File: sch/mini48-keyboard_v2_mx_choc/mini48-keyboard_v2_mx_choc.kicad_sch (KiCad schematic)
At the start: 1 part, among them U1 Pico

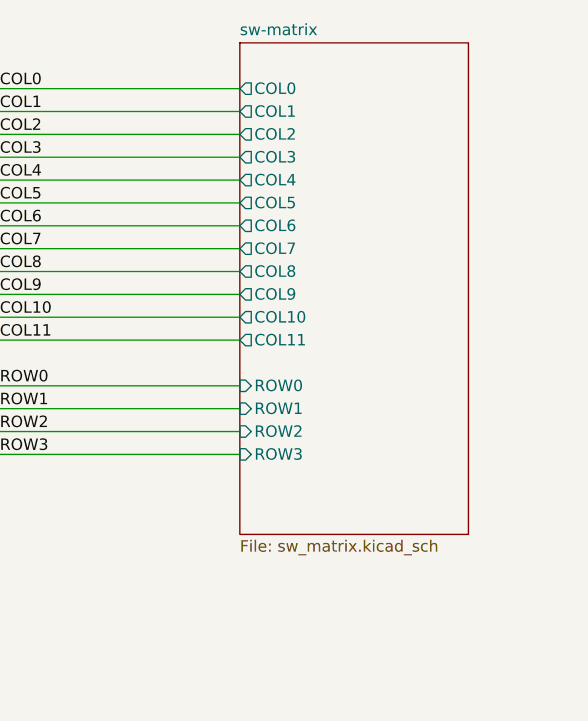
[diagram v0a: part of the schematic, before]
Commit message: スイッチのシート名を変更しました。
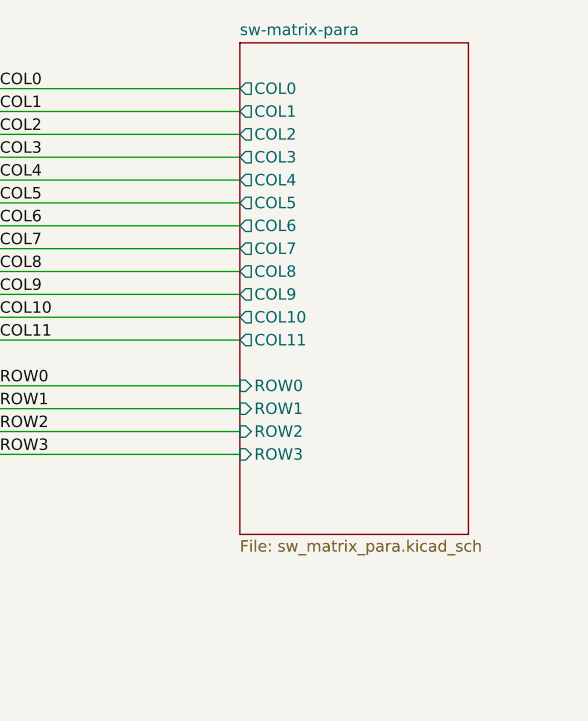
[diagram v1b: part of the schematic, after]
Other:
- sheet sw-matrix renamed sw-matrix-para
- sheet sw-matrix-para: file sw_matrix.kicad_sch -> sw_matrix_para.kicad_sch
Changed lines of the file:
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@@
 			(color 0 0 0 0.0000)
 		)
-		(property "Sheetname" "sw-matrix"
+		(property "Sheetname" "sw-matrix-para"
 			(at 204.47 36.1184 0)
 			(effects
@@
 			)
 		)
-		(property "Sheetfile" "sw_matrix.kicad_sch"
+		(property "Sheetfile" "sw_matrix_para.kicad_sch"
 			(at 204.47 92.0246 0)
 			(effects

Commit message: 基板上にUSB type-cのコネクタを実装しました。 picoのTPとジャンパ配線します。
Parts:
- added H1, H10, H11, H12, H2, H3, H4, H5, H6, H7, H8, H9: MountingHole, my_keyswitch:my_MountingHole_3.2mm_M3, symbol Mechanical:MountingHole
- U1: footprint my_pico:pico_no_dbg_th_p0.85 -> my_pico:pico_no_dbg_smd_th_p0.85
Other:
- added sheet usb type-c (usb_type_c.kicad_sch)

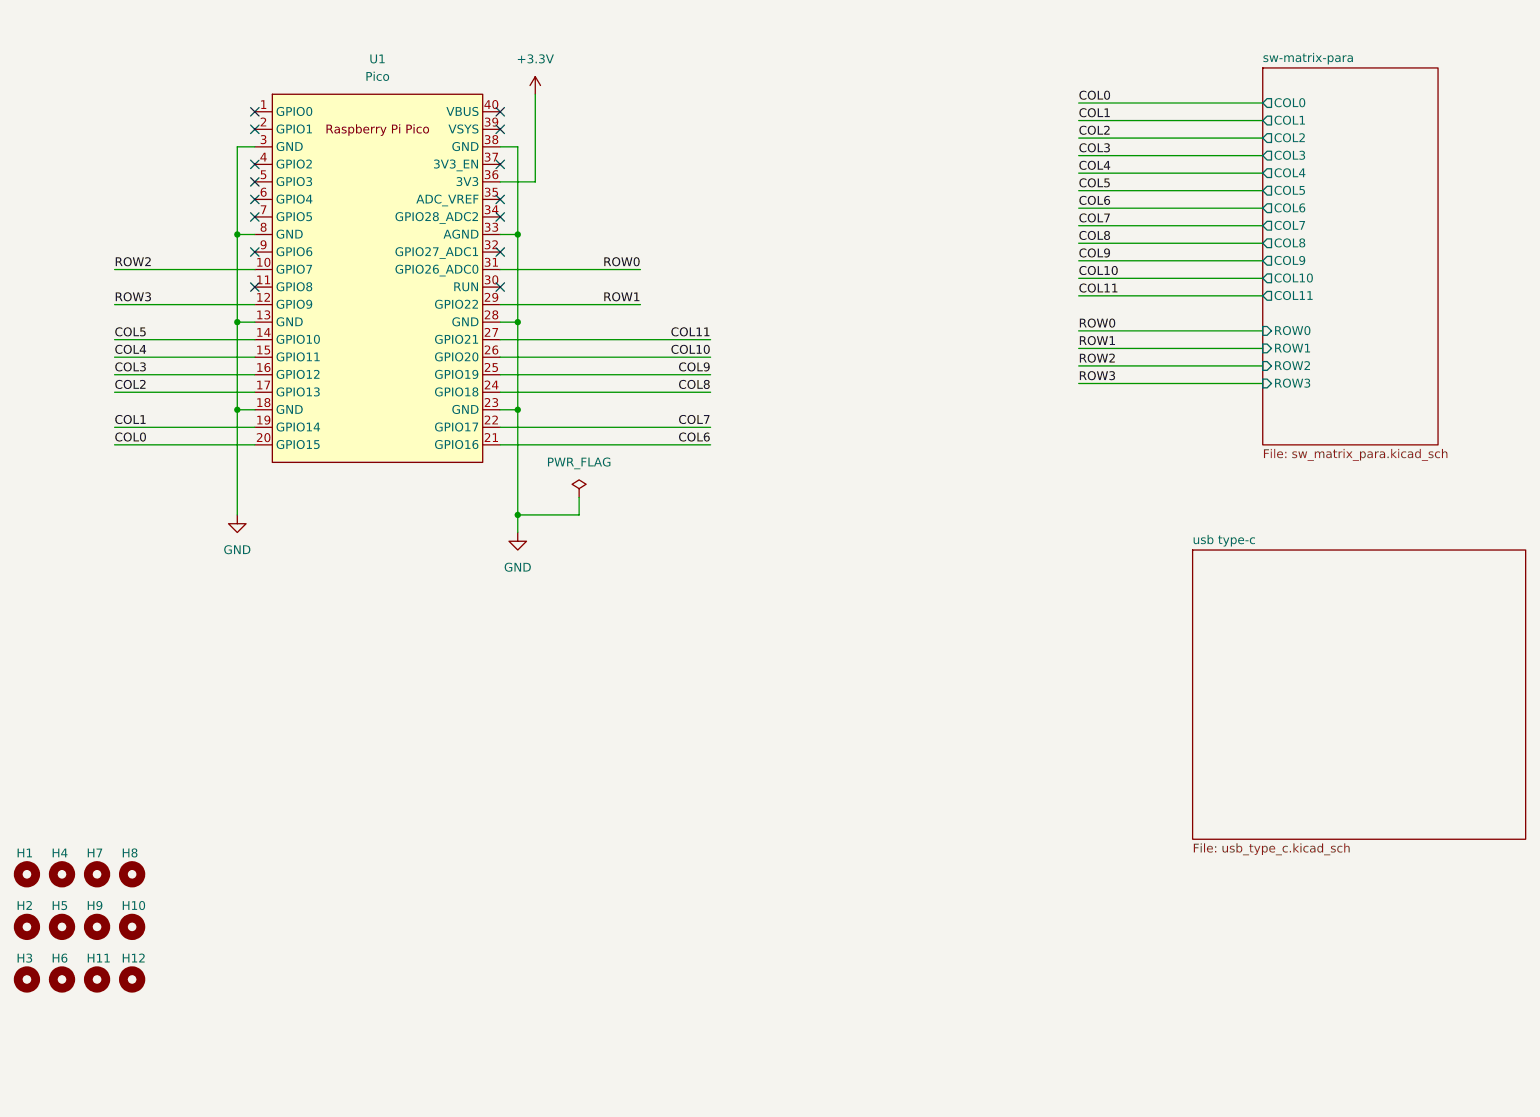
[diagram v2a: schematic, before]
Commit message: トラックポイント用の回路を追加しました。
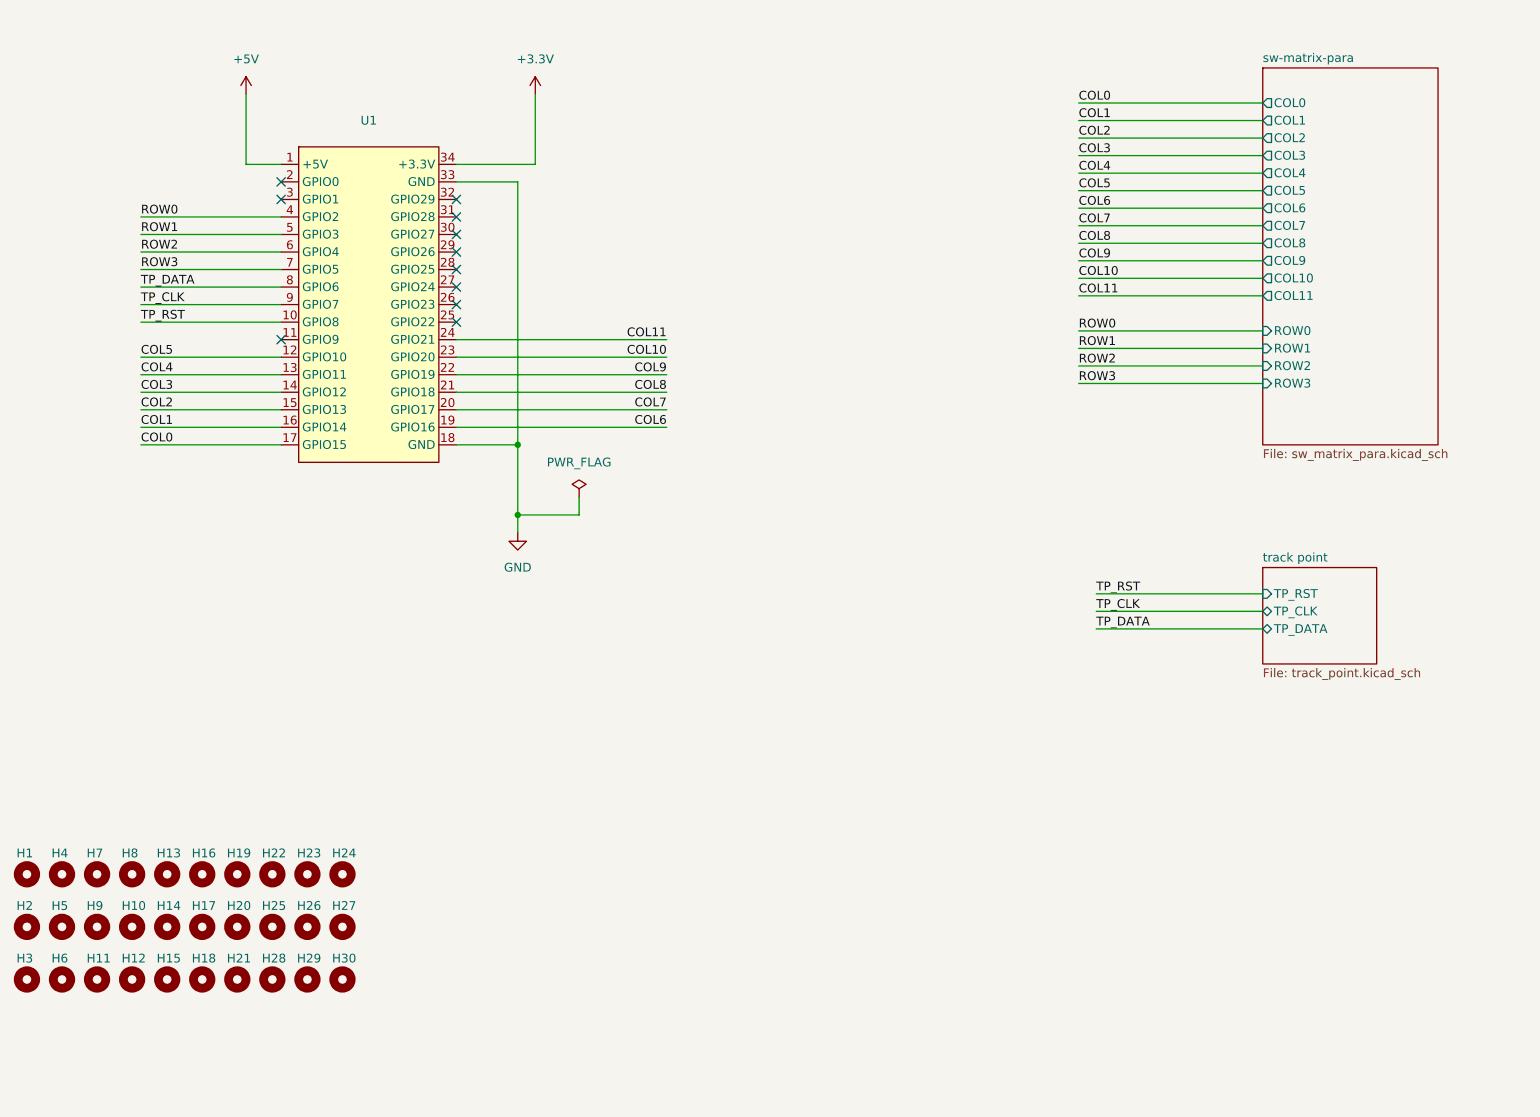
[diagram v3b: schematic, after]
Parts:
- removed U1: Pico, my_pico:pico_no_dbg_smd_th_p0.85, symbol my_pico:my_pico_no_dbg
- added H13, H14, H15, H16, H17, H18, H19, H20, H21, H22, H23, H24, H25, H26, H27, H28, H29, H30: MountingHole, my_keyswitch:my_MountingHole_3.2mm_M3, symbol Mechanical:MountingHole
- added U1: ~, ae-rp2040:AE-RP2040, symbol ae-rp2040:AE-RP2040
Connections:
- net +3.3V: now also U1.34 (+3.3V)
- net COL0: now also U1.17 (GPIO15)
- net COL1: now also U1.16 (GPIO14)
- net COL10: now also U1.23 (GPIO20)
- net COL11: now also U1.24 (GPIO21)
- net COL2: now also U1.15 (GPIO13)
- net COL3: now also U1.14 (GPIO12)
- net COL4: now also U1.13 (GPIO11)
- net COL5: now also U1.12 (GPIO10)
- net COL6: now also U1.19 (GPIO16)
- net COL7: now also U1.20 (GPIO17)
- net COL8: now also U1.21 (GPIO18)
- net COL9: now also U1.22 (GPIO19)
- net GND: now also U1.18 (GND), U1.33 (GND)
- net ROW0: now also U1.4 (GPIO2)
- net ROW1: now also U1.5 (GPIO3)
- net ROW2: now also U1.6 (GPIO4)
- net ROW3: now also U1.7 (GPIO5)
- new net +5V: U1.1 (+5V)
- new net TP_CLK: U1.9 (GPIO7)
- new net TP_DATA: U1.8 (GPIO6)
- new net TP_RST: U1.10 (GPIO8)
- no-connect marks 15 -> 11
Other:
- removed sheet usb type-c
- added sheet track point (track_point.kicad_sch)

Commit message: やっぱり標準のマイコンはpicoのピン配に合わせる。
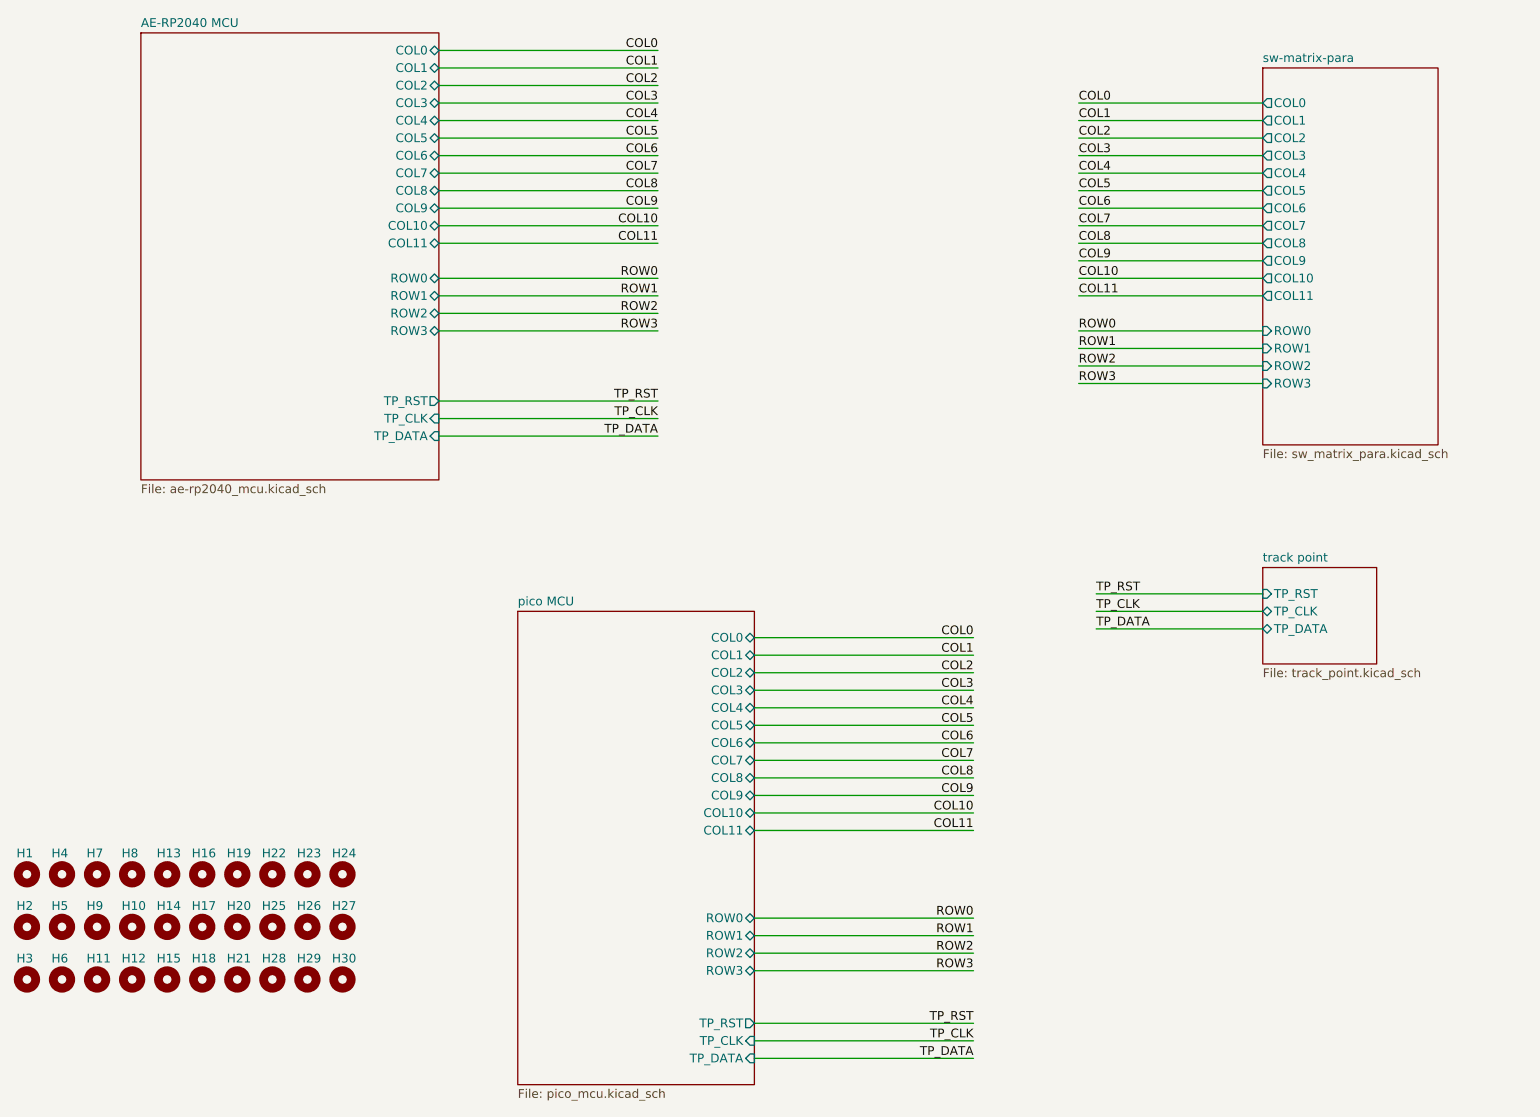
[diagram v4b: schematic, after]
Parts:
- removed U1: ~, ae-rp2040:AE-RP2040, symbol ae-rp2040:AE-RP2040
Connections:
- no-connect marks 11 -> 0
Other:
- added sheet AE-RP2040 MCU (ae-rp2040_mcu.kicad_sch)
- added sheet pico MCU (pico_mcu.kicad_sch)

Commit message: ひとまずすべての未配線をなくした版です。 配線は整えていません。 また、GNDプレーンのビアは打っていません。
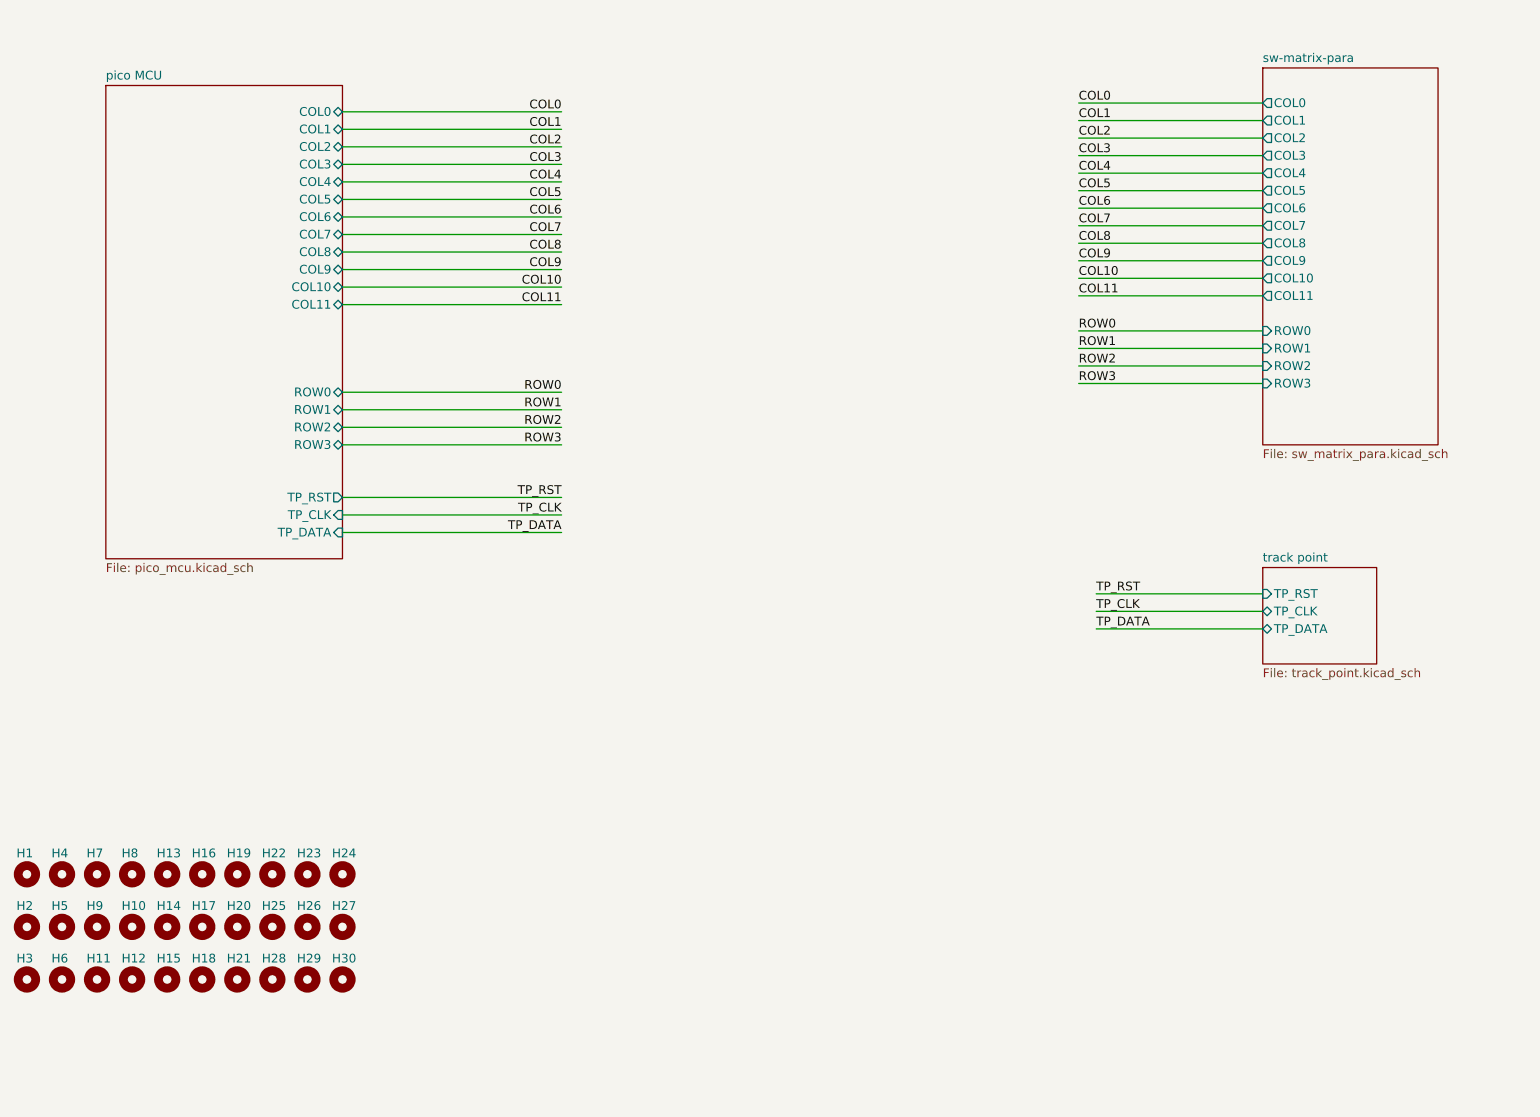
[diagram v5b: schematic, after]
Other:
- removed sheet AE-RP2040 MCU

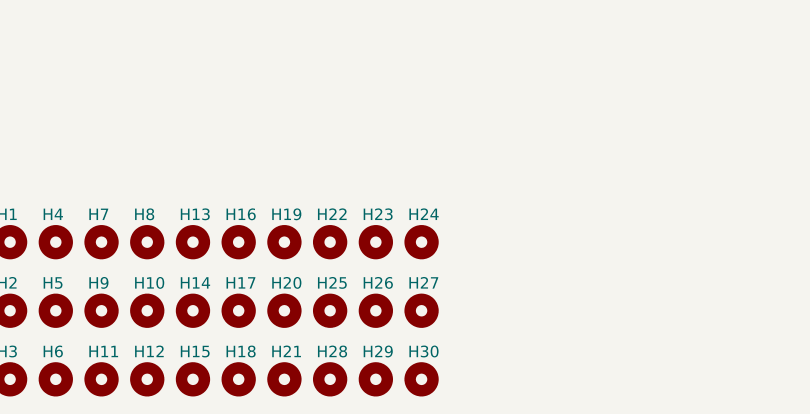
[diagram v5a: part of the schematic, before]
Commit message: picoの位置を左上に変更しました。
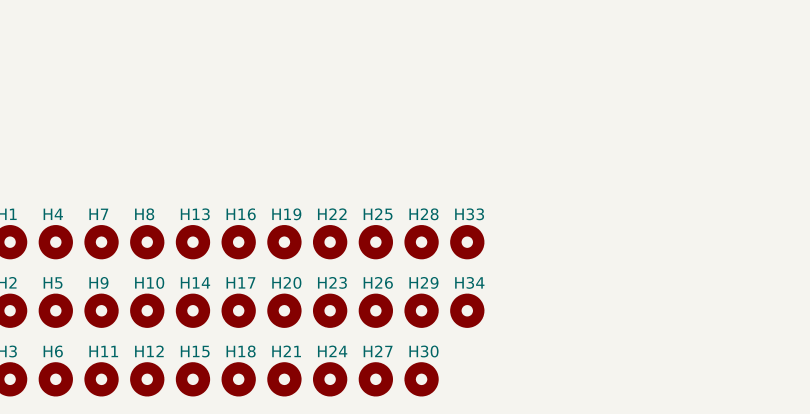
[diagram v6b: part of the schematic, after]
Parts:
- added H33, H34: MountingHole, my_keyswitch:my_MountingHole_3.2mm_M3, symbol Mechanical:MountingHole
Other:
- moved on the sheet: H23, H24, H25, H27, H28, H29
